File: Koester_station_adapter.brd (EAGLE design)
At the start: 50 x 69 mm, 12 parts, among them CON1 Speaker

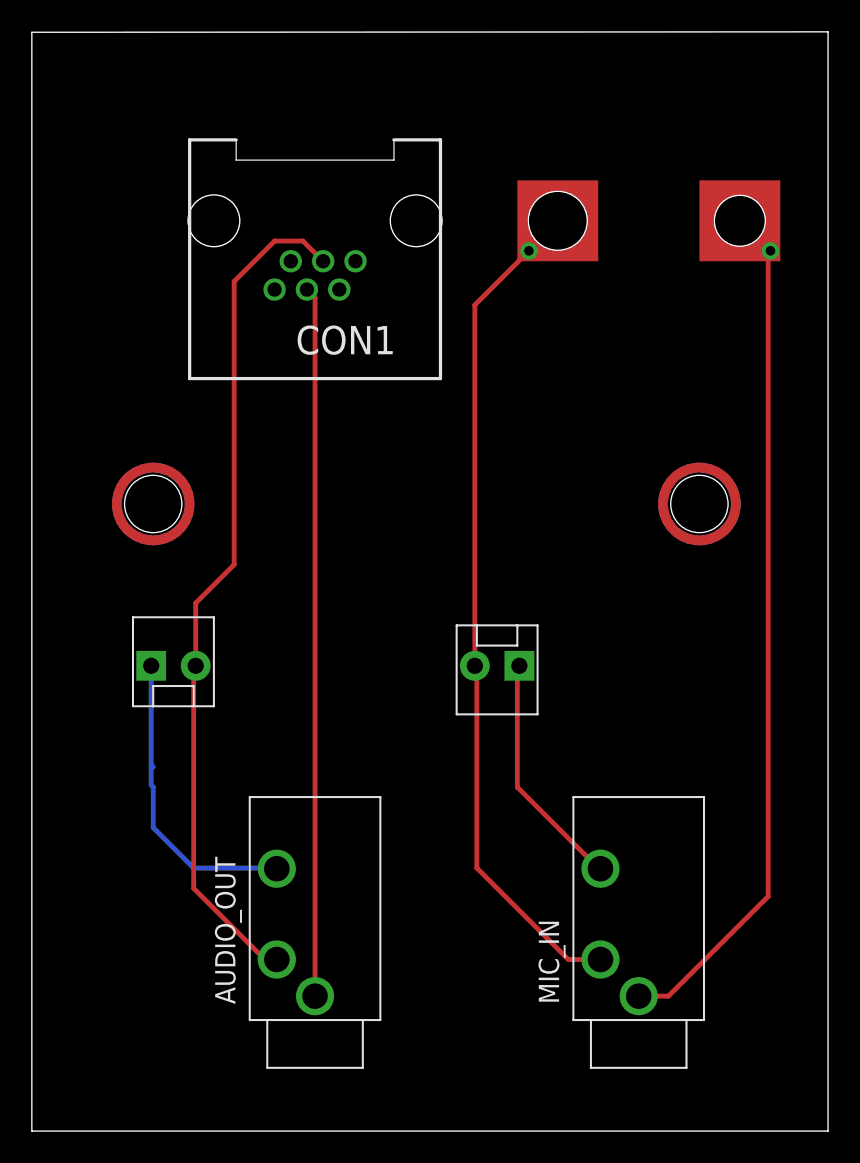
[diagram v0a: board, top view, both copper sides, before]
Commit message: Version 1.2
Replaced brass screws on board with 6mm terminal strip
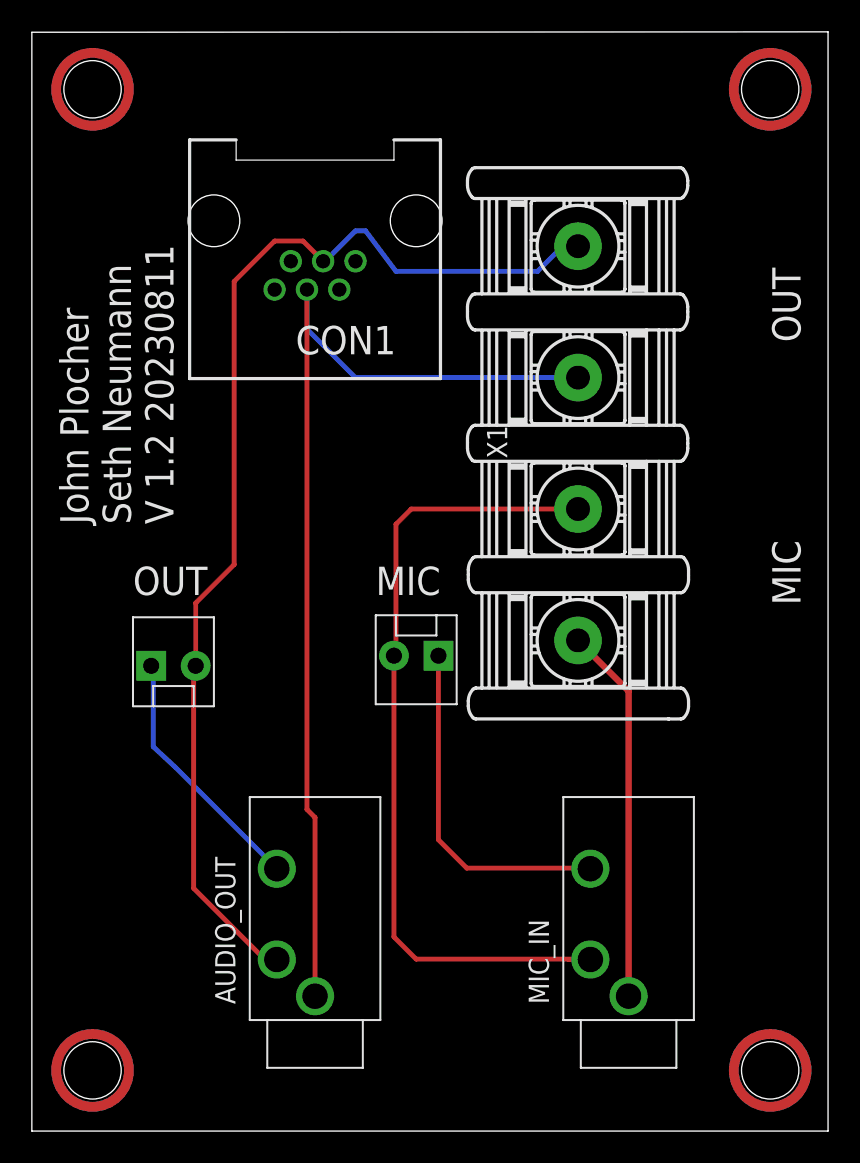
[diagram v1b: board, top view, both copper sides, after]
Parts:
- added X1: 5202-04-N-02, con-ebyelectro:5202-04-N-02
- U$3: value Mic Tip -> MOUNTINGHOLE; device SPCoast:TP06 -> SPCoast:MOUNTINGHOLE
- U$4: value TP -> MOUNTINGHOLE; device SPCoast:TP06 -> SPCoast:MOUNTINGHOLE
- moved U$3 58.3 mm to (3.81, 3.81)
- moved U$1 35.8 mm to (46.4, 3.81)
- moved U$2 26.3 mm to (3.81, 65.4)
- moved U$4 10.1 mm to (46.4, 65.4)
- moved JP2 5.12 mm to (25.4, 29.8)
- moved U$6 3.24 mm to (2.16, 8.00)
- moved U$5 3.17 mm to (2.79, 8.00)
- moved MIC_IN 0.63 mm to (37.5, 14.0)
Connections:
- removed net N$1: AUDIO_OUT.TIP, CON1.4, JP1.2
- removed net N$2: AUDIO_OUT.GND, CON1.3
- removed net N$4: MIC_IN.GND, U$4.P$1
- removed net N$5: JP2.2, MIC_IN.TIP, U$3.P$1
- new net MIC_SLEEVE: MIC_IN.GND, X1.1
- new net MIC_TIP: JP2.2, MIC_IN.TIP, X1.2
- new net OUT_SLEEVE: AUDIO_OUT.GND, CON1.3, X1.3
- new net OUT_TIP: AUDIO_OUT.TIP, CON1.4, JP1.2, X1.4
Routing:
- net OUT_TIP: track 0.00 -> 71.6 mm
- net OUT_SLEEVE: track 0.00 -> 65.3 mm
- net N$1: track 53.4 -> 0.00 mm
- net MIC_TIP: track 0.00 -> 53.3 mm
- net N$4: track 51.3 -> 0.00 mm
- net N$5: track 50.3 -> 0.00 mm
- net N$2: track 44.6 -> 0.00 mm
- net MIC_SLEEVE: track 0.00 -> 23.7 mm
- net N$6: track 15.0 -> 23.0 mm
- net N$3: track 19.2 -> 16.0 mm
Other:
- board text added: "John Plocher Seth Neumann V 1.2 20230811"
- board text added: "MIC"
- board text added: "Mic/Spkr adapter"
- board text added: "OUT"
- board text removed: "Candlestick phone adapter"
- board text removed: "Mic + Mic -"
